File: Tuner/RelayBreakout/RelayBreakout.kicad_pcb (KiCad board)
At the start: 2 copper layers, 100 x 100 mm, 121 parts, among them J1 Conn_01x01, J10 Conn_01x02, J11 Conn_01x02, J12 Conn_01x02, J13 Conn_01x02, J14 Conn_01x02, J15 Conn_01x02, J16 Conn_01x02, J17 Conn_01x02, J18 Conn_01x02, J19 Conn_01x02, J2 Conn_01x01, J20 Conn_01x02, J21 Conn_01x02, J3 Conn_01x01, J4 Conn_01x01, J5 Conn_02x16_Odd_Even, J6 Conn_01x02, J7 Conn_01x02, J8 Conn_01x02, J9 Conn_01x02

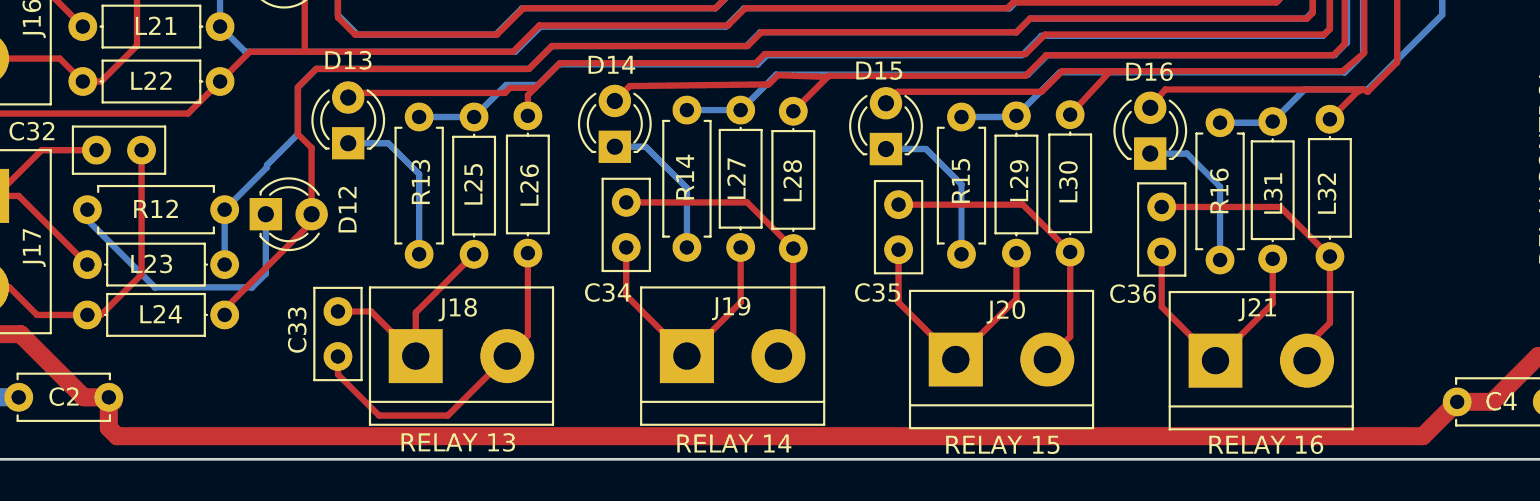
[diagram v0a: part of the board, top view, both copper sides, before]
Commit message: Added Bill of Materials to PCBs
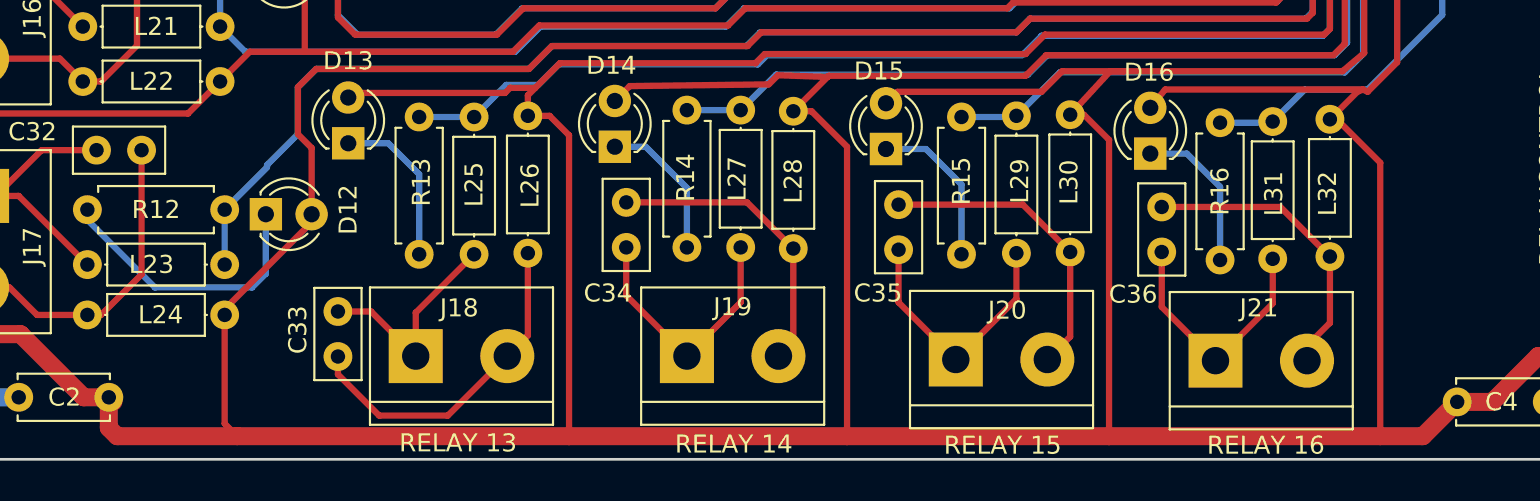
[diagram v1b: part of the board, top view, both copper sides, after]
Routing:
- net +12V: track 1928.0 -> 2012.5 mm
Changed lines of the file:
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@@
     (thickness 1.6)
     (drawings 22)
-    (tracks 920)
+    (tracks 939)
     (zones 0)
     (modules 121)
@@
     (pad_to_mask_clearance 0.2)
     (aux_axis_origin 0 0)
-    (visible_elements FFFFFF7F)
+    (visible_elements 7FFFFFFF)
     (pcbplotparams
       (layerselection 0x010f0_80000001)
@@
   (segment (start 146.812 146.812) (end 147 147) (width 1) (layer B.Cu) (net 4))
   (segment (start 146.812 146.812) (end 147 147) (width 0.5) (layer B.Cu) (net 4))
+  (segment (start 68.834 141.986) (end 68.834 148.0185) (width 0.35) (layer F.Cu) (net 5) (status 400000))
+  (segment (start 68.834 148.0185) (end 69.5325 148.717) (width 0.35) (layer F.Cu) (net 5))
+  (segment (start 130.175 131.1275) (end 130.556 131.1275) (width 0.35) (layer F.Cu) (net 5) (status C00000))
+  (segment (start 130.556 131.1275) (end 132.969 133.5405) (width 0.35) (layer F.Cu) (net 5) (status 400000))
+  (segment (start 132.969 133.5405) (end 132.969 148.717) (width 0.35) (layer F.Cu) (net 5))
+  (segment (start 115.7605 130.8735) (end 116.5225 130.8735) (width 0.35) (layer F.Cu) (net 5) (status C00000))
+  (segment (start 116.5225 130.8735) (end 117.9195 132.2705) (width 0.35) (layer F.Cu) (net 5) (status 400000))
+  (segment (start 117.9195 132.2705) (end 117.9195 148.717) (width 0.35) (layer F.Cu) (net 5))
+  (segment (start 100.3935 130.683) (end 101.4095 130.683) (width 0.35) (layer F.Cu) (net 5) (status 400000))
+  (segment (start 103.378 132.6515) (end 103.378 148.717) (width 0.35) (layer F.Cu) (net 5))
+  (segment (start 101.4095 130.683) (end 103.378 132.6515) (width 0.35) (layer F.Cu) (net 5))
+  (segment (start 85.6615 130.937) (end 86.868 130.937) (width 0.35) (layer F.Cu) (net 5) (status 400000))
+  (segment (start 87.9475 132.0165) (end 87.9475 148.717) (width 0.35) (layer F.Cu) (net 5))
+  (segment (start 86.868 130.937) (end 87.9475 132.0165) (width 0.35) (layer F.Cu) (net 5))
   (segment (start 124.333 70.0405) (end 124.333 68.453) (width 0.35) (layer F.Cu) (net 5))
   (segment (start 71.4375 116.1796) (end 71.4375 113.36274) (width 0.35) (layer F.Cu) (net 5))
@@
   (segment (start 133.9088 127.9652) (end 132.2705 129.6035) (width 0.35) (layer F.Cu) (net 5))
   (segment (start 62.404 146.558) (end 62.404 148.256) (width 1) (layer F.Cu) (net 5))
-  (segment (start 135.335 148.717) (end 137.24 146.812) (width 1) (layer F.Cu) (net 5))
-  (segment (start 62.865 148.717) (end 135.335 148.717) (width 1) (layer F.Cu) (net 5))
+  (segment (start 62.865 148.717) (end 69.5325 148.717) (width 1) (layer F.Cu) (net 5))
   (segment (start 62.404 148.256) (end 62.865 148.717) (width 1) (layer F.Cu) (net 5))
+  (segment (start 69.5325 148.717) (end 87.9475 148.717) (width 1) (layer F.Cu) (net 5))
+  (segment (start 135.335 148.717) (end 137.24 146.812) (width 1) (layer F.Cu) (net 5))
+  (segment (start 103.378 148.717) (end 117.9195 148.717) (width 1) (layer F.Cu) (net 5))
+  (segment (start 117.9195 148.717) (end 132.969 148.717) (width 1) (layer F.Cu) (net 5))
+  (segment (start 132.969 148.717) (end 135.335 148.717) (width 1) (layer F.Cu) (net 5))
+  (segment (start 87.9475 148.717) (end 103.378 148.717) (width 1) (layer F.Cu) (net 5))
   (segment (start 72.1995 68.3895) (end 72.1995 64.8335) (width 0.35) (layer F.Cu) (net 5))
   (segment (start 69.342 57.15) (end 69.342 50.8508) (width 0.35) (layer F.Cu) (net 5))
